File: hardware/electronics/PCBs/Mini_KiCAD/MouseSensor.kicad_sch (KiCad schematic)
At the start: 8 parts, among them U2 ADNS-5050

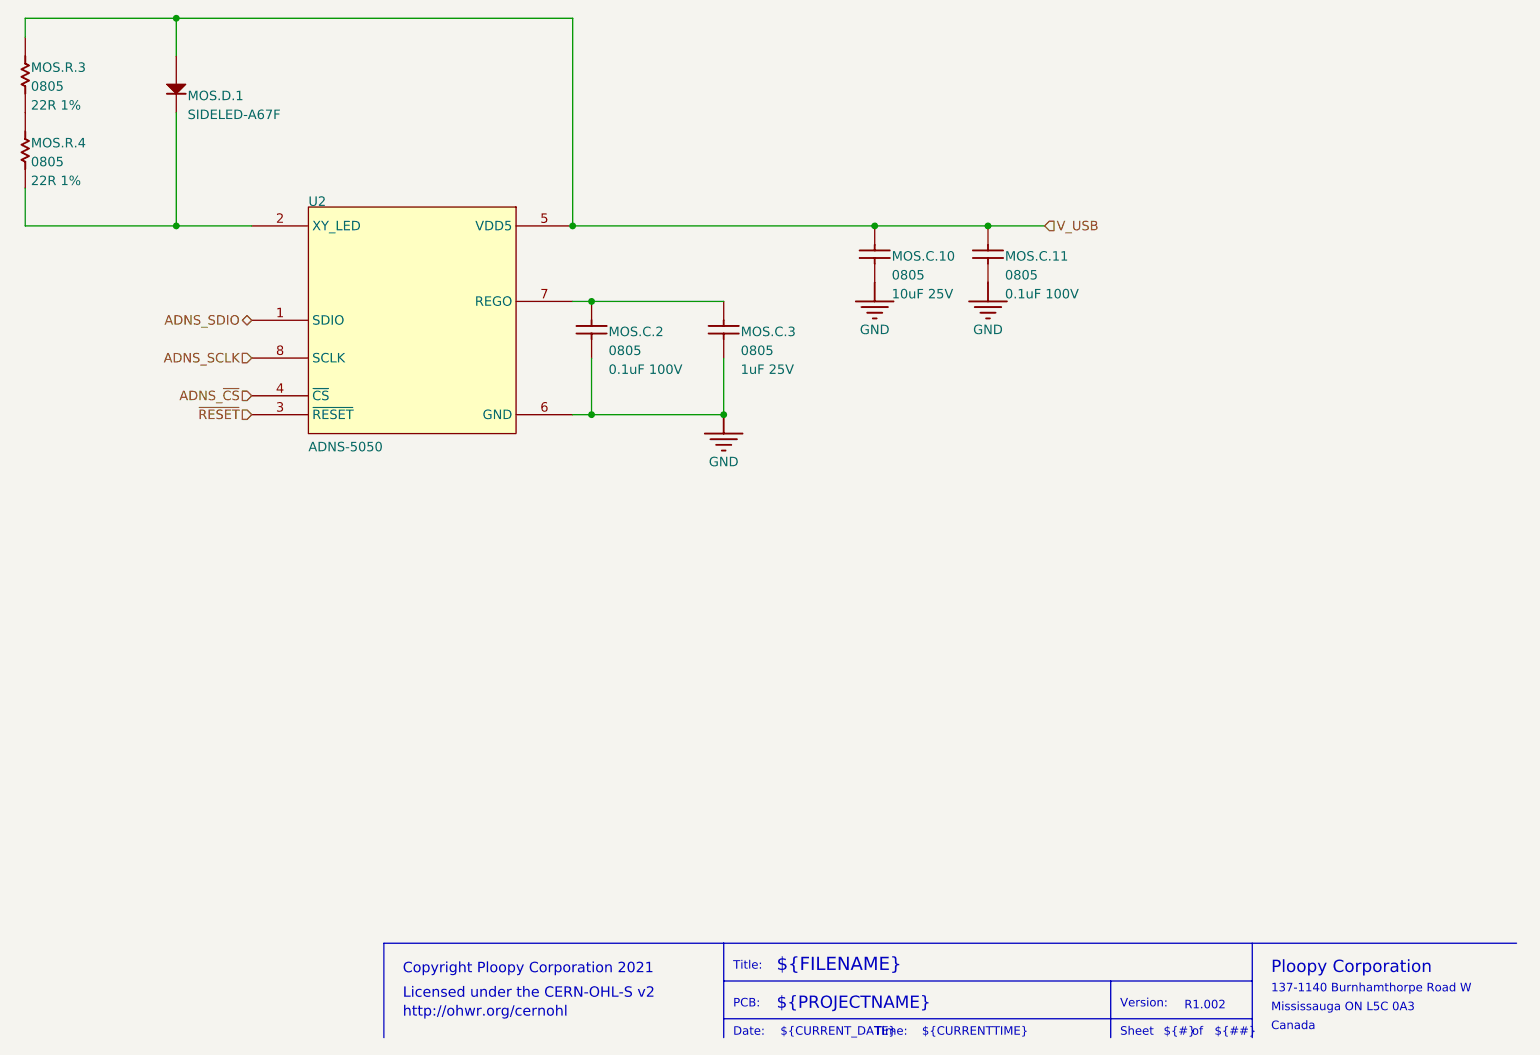
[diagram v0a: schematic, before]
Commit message: Initial commit of the PCB project file replacing the ADNS-5050 with PMW3360, referencing the schematic of the Ploopy Classic.
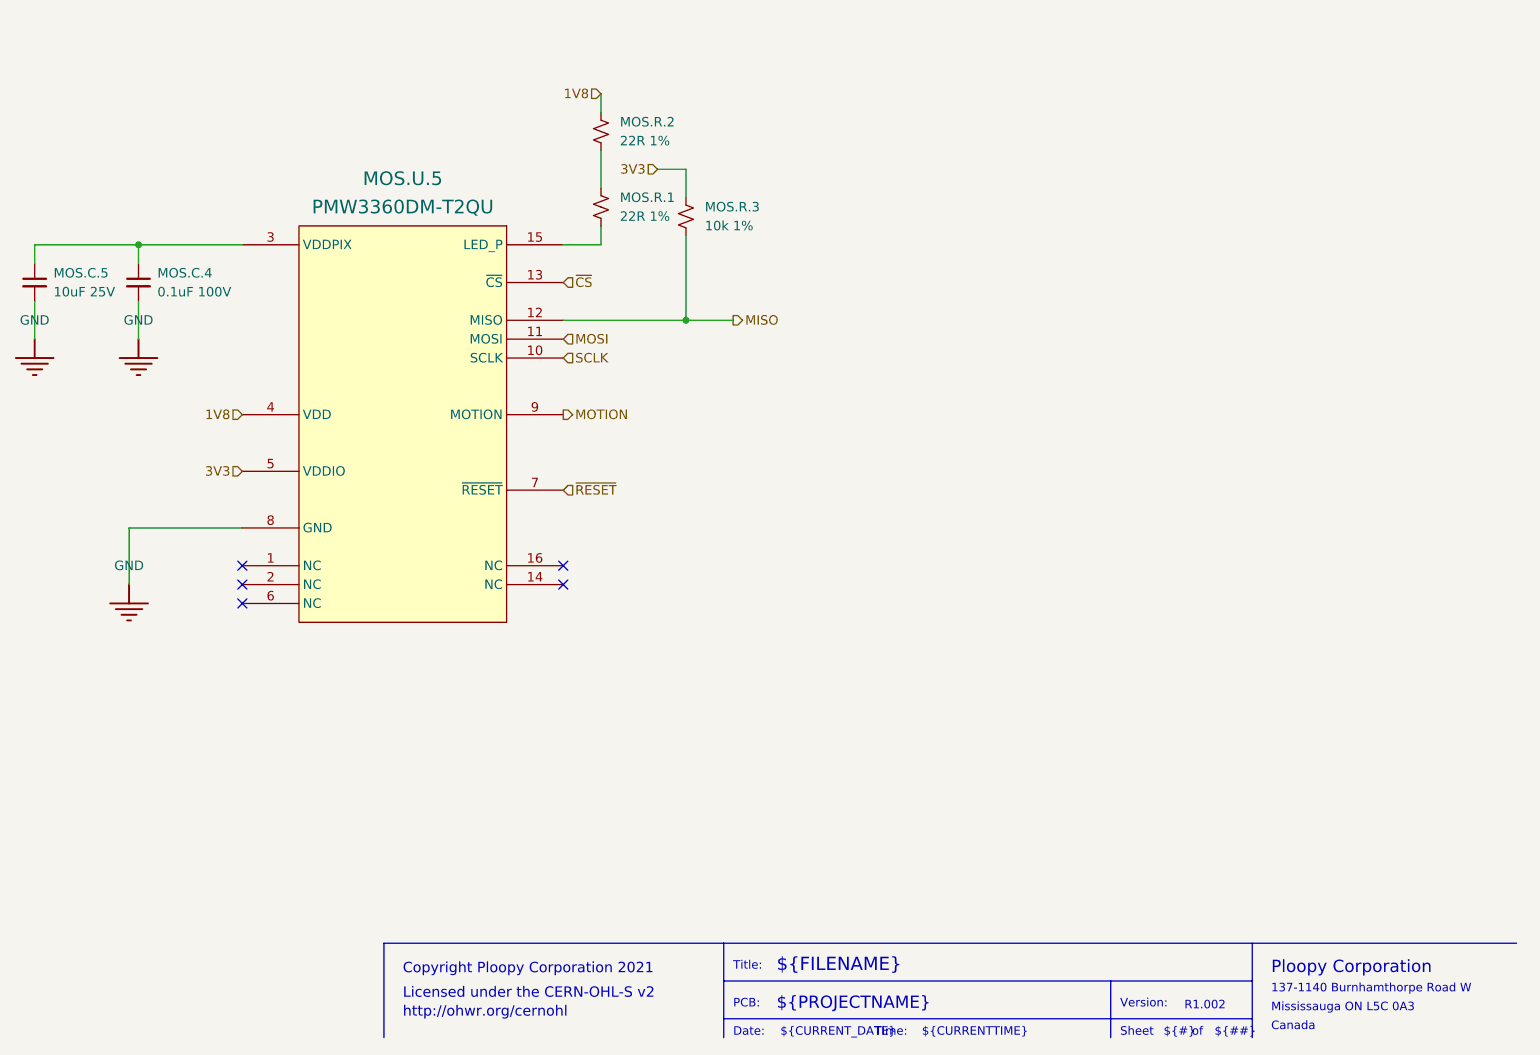
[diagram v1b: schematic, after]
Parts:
- removed MOS.C.10: 0805, 0805 - TALL, symbol Mini-altium-import:MOS_1_Cap 10uF 25V
- removed MOS.C.11, MOS.C.2: 0805, 0805 - TALL, symbol Mini-altium-import:MOS_1_Cap 0.1uF 100V
- removed MOS.C.3: 0805, 0805 - TALL, symbol Mini-altium-import:MOS_1_Cap 1uF 25V
- removed MOS.D.1: SIDELED-A67F, SIDELED-A67F, symbol Mini-altium-import:MOS_1_SIDELED-A67F
- removed MOS.R.3, MOS.R.4: 0805, 0805, symbol Mini-altium-import:MOS_1_Res 22R 1% 0805
- removed U2: ADNS-5050, ADNS-5050, symbol Mini-altium-import:MOS_0_ADNS-5050
- added MOS.C.4: 0.1uF 100V, Chip_Passives.PcbLib:0805, symbol Device:C_Small
- added MOS.C.5: 10uF 25V, Chip_Passives.PcbLib:0805, symbol Device:C_Small
- added MOS.R.1, MOS.R.2: 22R 1%, Chip_Passives.PcbLib:0805, symbol Device:R_Small_US
- added MOS.R.3: 10k 1%, Chip_Passives.PcbLib:0805, symbol Device:R_Small_US
- added MOS.U.5: PMW3360DM-T2QU, OptoElectronics:PMW3360DM-T2QU, symbol OptoElectronics.PcbLib:PMW3360DM-T2QU
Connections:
- net GND: now also MOS.C.4.2, MOS.C.5.2, MOS.U.5.8 (GND)
- net ~{RESET}: now also MOS.U.5.7 (~{RESET})
- new net: MOS.R.1.2, MOS.U.5.15 (LED_P)
- new net: MOS.C.4.1, MOS.C.5.1, MOS.U.5.3 (VDDPIX)
- new net: MOS.R.1.1, MOS.R.2.2
- new net 1V8: MOS.R.2.1, MOS.U.5.4 (VDD)
- new net 3V3: MOS.R.3.1, MOS.U.5.5 (VDDIO)
- new net MISO: MOS.R.3.2, MOS.U.5.12 (MISO)
- new net MOSI: MOS.U.5.11 (MOSI)
- new net MOTION: MOS.U.5.9 (MOTION)
- new net SCLK: MOS.U.5.10 (SCLK)
- new net ~{CS}: MOS.U.5.13 (~{CS})
- no-connect marks 0 -> 5
